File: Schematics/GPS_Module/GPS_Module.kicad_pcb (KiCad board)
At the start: 4 copper layers, 69.5 x 60 mm, 68 parts, among them J1 470804001, J2 SWD_01x04_Pin, J4 Stack Male Edge Connector, J6 USB_B_Micro, Q1 AO3400A, SW1 SW_STM_RESET, SW2 SW_STM_BOOT_MODE, U1 STM32F103CBTx, U10 AMS1117-3.3, U3 W25Q128JVS, U4 LM66100DCKR, U5 LM66100DCKR, U6 LM66100DCKR, U7 ACS70331EOLC, U9 ISO1042BQDWVR, Y1 X322516MMB4SI

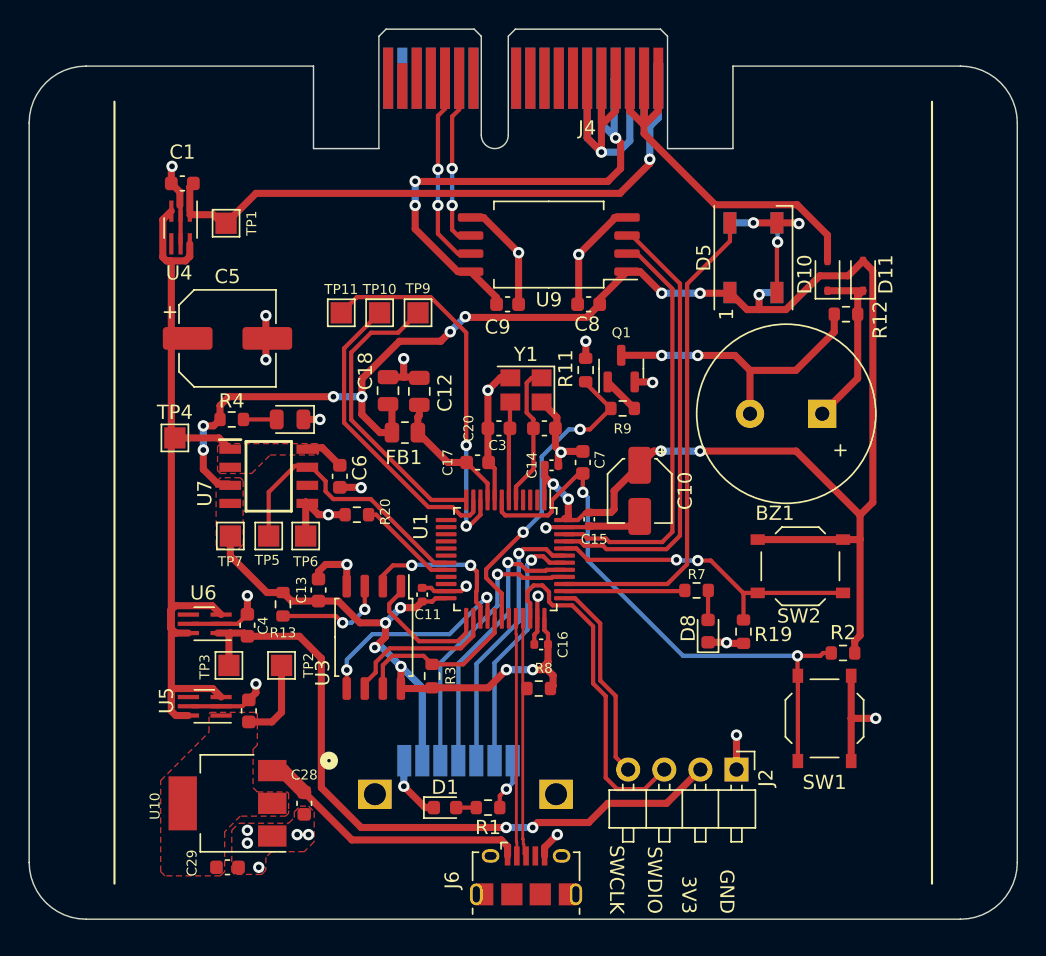
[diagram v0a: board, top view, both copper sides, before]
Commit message: finished silkscreen for GPS module
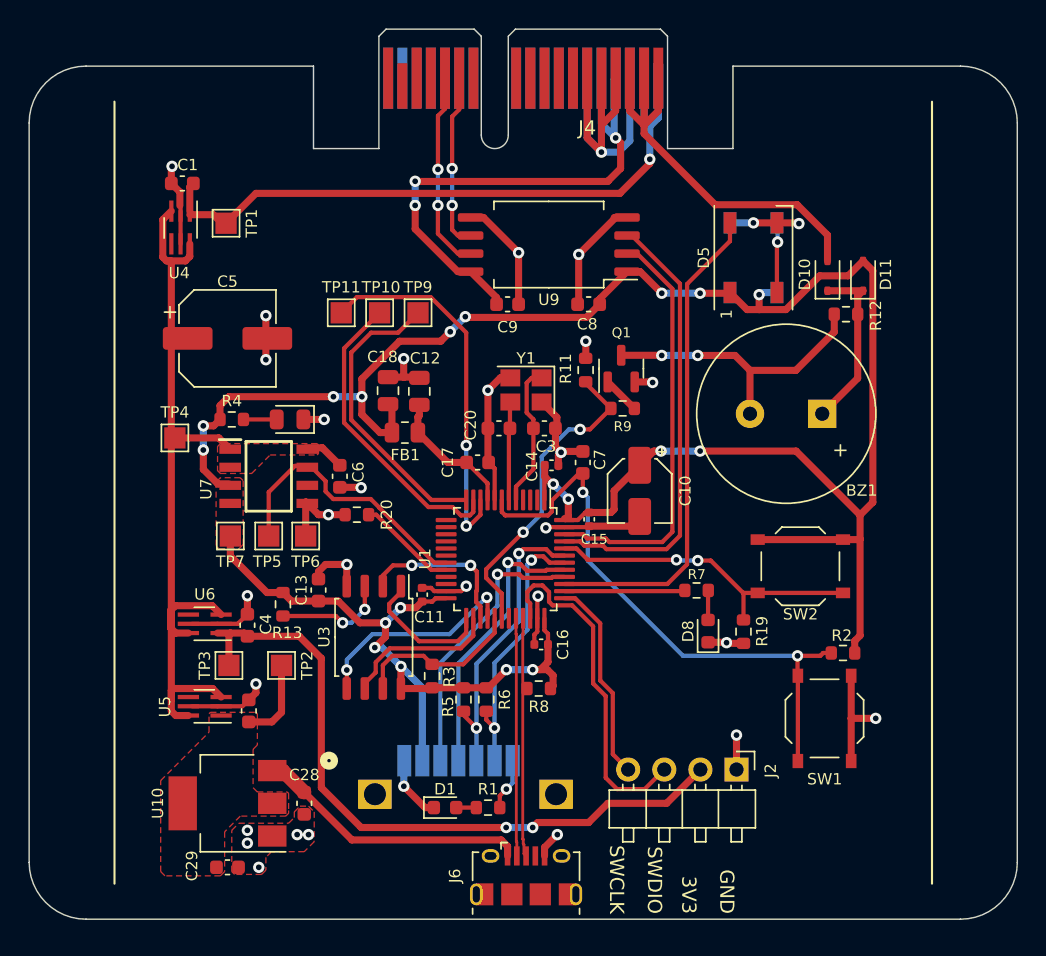
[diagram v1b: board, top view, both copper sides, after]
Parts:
- added R5: 2.2k, Resistor_SMD:R_0603_1608Metric, F.Cu at (52.7, 64.7)
- added R6: 2.2k, Resistor_SMD:R_0603_1608Metric, F.Cu at (54.3, 64.7)
- J1: value 470804001 -> SATA Conn. (Male)
- U1: value STM32F103CBTx -> STM32F103CBT6
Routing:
- net SDA_GPS: track 19.3 -> 20.9 mm, vias 1 -> 2
- net SCL_GPS: track 17.8 -> 19.2 mm, vias 1 -> 2

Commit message: PCB Adjustments + Add USB-C port (DRC pass)
- Rerouted several traces to reduce via hopping
- Routed CANBUS wires as differential pair
- Rearranged some items
- Swapped USB-MicroB port for USB-C port
- Added silkscreen labels
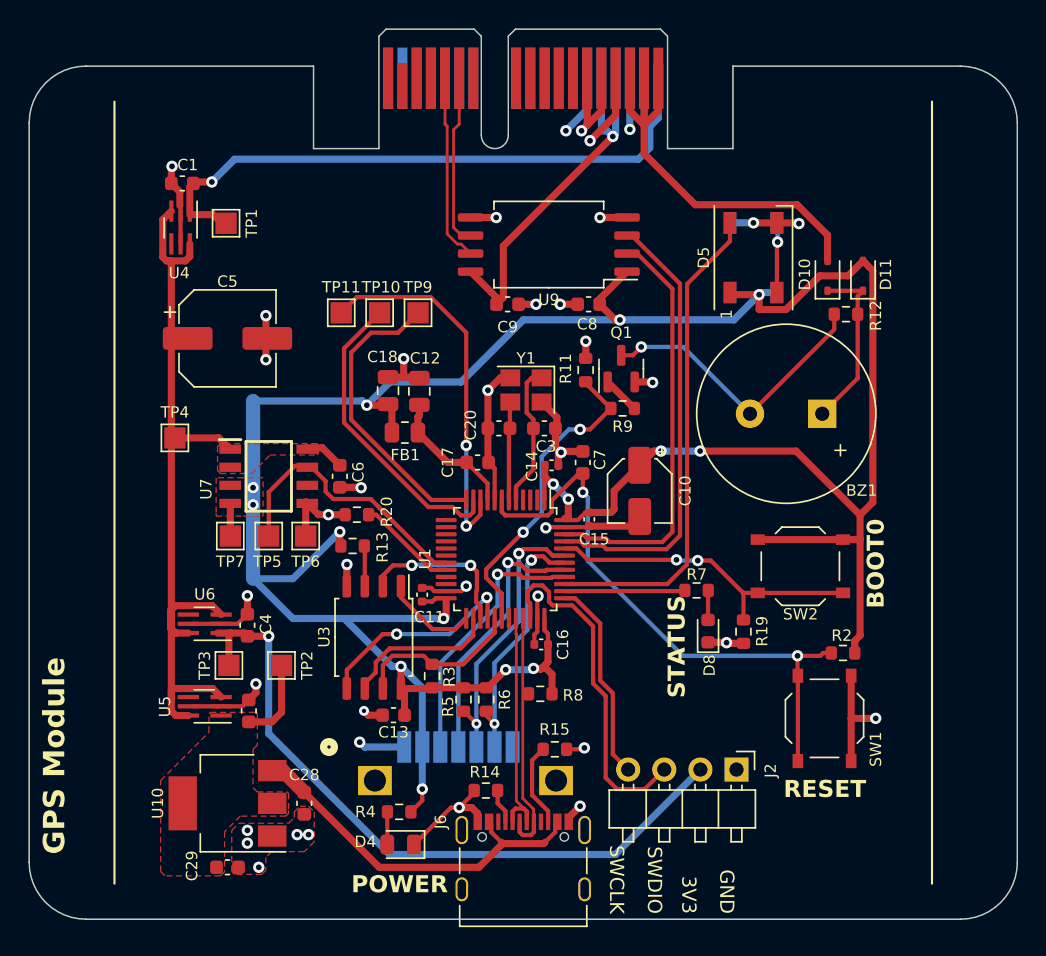
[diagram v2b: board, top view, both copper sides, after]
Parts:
- removed D1: PPS_LED (YLW), LED_SMD:LED_0603_1608Metric
- removed R1: 560R, Resistor_SMD:R_0603_1608Metric
- added R14: 5.1k, Resistor_SMD:R_0603_1608Metric, F.Cu at (54.3, 71.1)
- added R15: 5.1k, Resistor_SMD:R_0603_1608Metric, F.Cu at (59.1, 68.2)
- J6: value USB_B_Micro -> USB_C_Female_USB2_Small; footprint Connector_USB:USB_Micro-B_Amphenol_10118194_Horizontal -> footprints:USB_C_DB-108PWB
- moved D4 30.9 mm to (48.3, 74.9)
- moved R4 30.0 mm to (48.2, 72.6), turned to 0 degrees
- moved C13 10.3 mm to (47.8, 65.8), turned to 180 degrees
- moved R13 6.39 mm to (44.9, 53.9), turned to 180 degrees
- moved J6 1.31 mm to (56.9, 75.8)
- moved J1 0.96 mm to (52.8, 72.9)
- moved R8 0.39 mm to (58.1, 64.3), turned to 180 degrees
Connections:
- J1 pad 7: Net-(J1-Pad7) -> unconnected-(J1-Pad7)
- R8 pad 1: USB_D+ -> +3.3V
- R8 pad 2: +3.3V -> USB_D+
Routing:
- net +3.3V: track 185.2 -> 206.1 mm, vias 19 -> 15
- net GND: track 136.4 -> 122.3 mm, vias 32 -> 38
- net +5V: track 37.6 -> 27.1 mm, vias 3 -> 1
- net /USB_5V: track 19.4 -> 26.5 mm
- net Net-(J6-CC2): track 0.00 -> 5.89 mm
- net Net-(U3-IO2): track 7.98 -> 2.84 mm, vias 2 -> 0
- net Net-(J1-Pad7): track 3.67 -> 0.00 mm, vias 1 -> 0
- net CS_FL: track 9.67 -> 6.63 mm
- net Net-(J6-CC1): track 0.00 -> 2.43 mm
- net Net-(D1-A): track 1.41 -> 0.00 mm
- net +BATT: track 29.0 -> 29.8 mm
- net CAN_H: track 14.0 -> 13.2 mm, vias 2 -> 0
- net USB_D-: track 16.7 -> 17.3 mm
- net V_SWD: track 48.9 -> 49.1 mm, vias 2 -> 1
- net CAN_L: track 12.3 -> 12.1 mm, vias 2 -> 0
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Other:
- board text added: "BOOT0"
- board text added: "GPS Module"
- board text added: "POWER"
- board text added: "RESET"
- board text added: "STATUS"

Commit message: Add silkscreen & final PCB adjustments
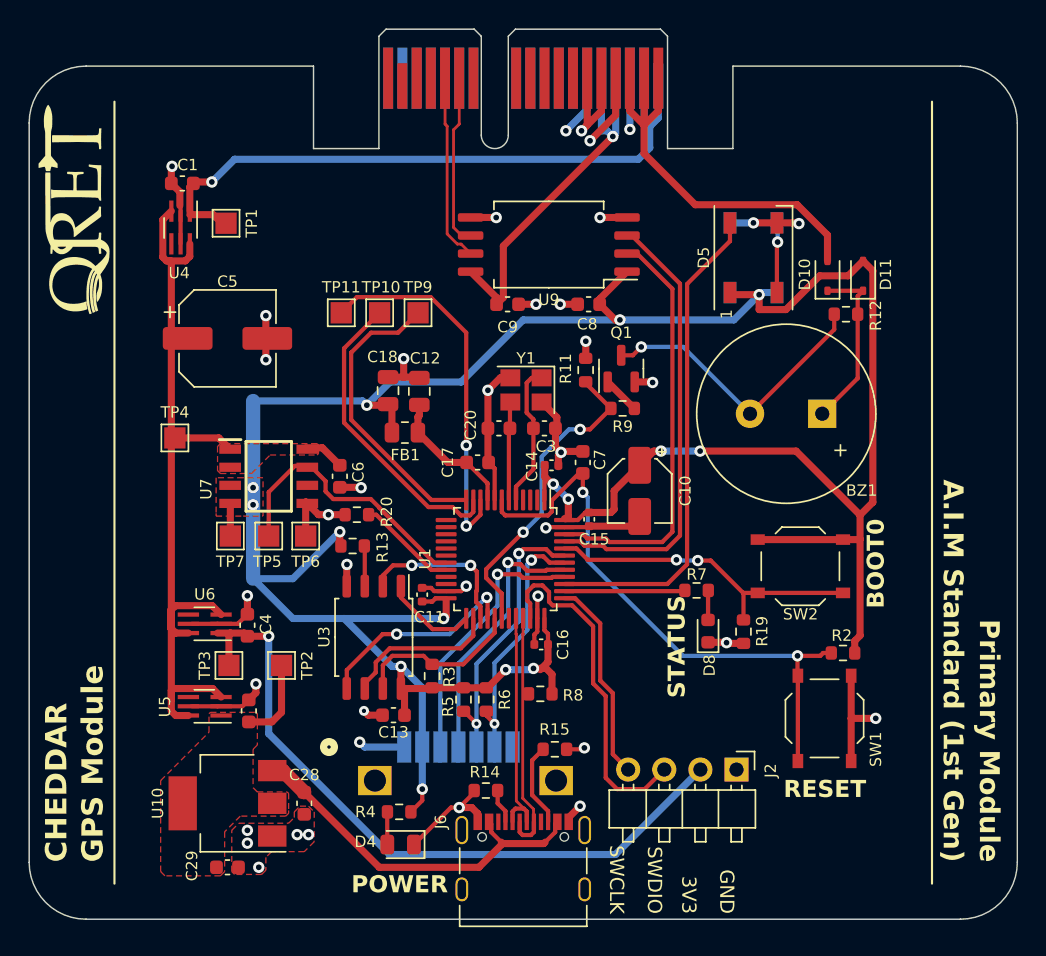
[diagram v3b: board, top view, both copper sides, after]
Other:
- board text added: "A.I.M Standard (1st Gen)"
- board text added: "CHEDDAR"
- board text added: "Cheddar Rev 1.0 QRET Mar 2024 Tristan Alderson Kennan Bays"
- board text added: "Primary Module"
- board text added: "To GPS Antenna Board"

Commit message: Updated Debug/PPS/Power LED resistors
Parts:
- R4: value 820R -> 1.2k
- R7: value 560R -> 680R
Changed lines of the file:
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@@
     (descr "Resistor SMD 0603 (1608 Metric), square (rectangular) end terminal, IPC_7351 nominal, (Body size source: IPC-SM-782 page 72, https://www.pcb-3d.com/wordpress/wp-content/uploads/ipc-sm-782a_amendment_1_and_2.pdf), generated with kicad-footprint-generator")
     (tags "resistor")
-    (property "LCSC" "C23253")
+    (property "LCSC" "C22765")
     (property "Sheetfile" "GPS_Module.kicad_sch")
     (property "Sheetname" "")
@@
         (effects (font (size 0.8 0.8) (thickness 0.1)))
     )
-    (fp_text value "820R" (at 0 1.43) (layer "F.Fab")
+    (fp_text value "1.2k" (at 0 1.43) (layer "F.Fab")
         (effects (font (size 1 1) (thickness 0.15)))
     )
@@
     (descr "Resistor SMD 0603 (1608 Metric), square (rectangular) end terminal, IPC_7351 nominal, (Body size source: IPC-SM-782 page 72, https://www.pcb-3d.com/wordpress/wp-content/uploads/ipc-sm-782a_amendment_1_and_2.pdf), generated with kicad-footprint-generator")
     (tags "resistor")
-    (property "LCSC" "C23204")
+    (property "LCSC" "C23228")
     (property "Sheetfile" "GPS_Module.kicad_sch")
     (property "Sheetname" "")
@@
         (effects (font (size 0.8 0.8) (thickness 0.1)))
     )
-    (fp_text value "560R" (at 0 1.43) (layer "F.Fab")
+    (fp_text value "680R" (at 0 1.43) (layer "F.Fab")
         (effects (font (size 1 1) (thickness 0.15)))
     )
@@
     (polygon
       (pts
-        (xy 22.15 20.15)
-        (xy 91.65 20.15)
+        (xy 22.15 14.15)
+        (xy 91.65 14.15)
         (xy 91.65 80.15)
         (xy 22.15 80.15)

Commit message: Final Revisions
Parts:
- moved D8 1.51 mm to (69.9, 61.4)
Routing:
- net Net-(D8-A): track 2.08 -> 3.59 mm
- net GND: track 122.3 -> 123.0 mm
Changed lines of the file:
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@@
   )
   (footprint "LED_SMD:LED_0603_1608Metric" (layer "F.Cu")
-    (at 69.9 59.8875 90)
+    (at 69.9 61.4 90)
     (descr "LED SMD 0603 (1608 Metric), square (rectangular) end terminal, IPC_7351 nominal, (Body size source: http://www.tortai-tech.com/upload/download/2011102023233369053.pdf), generated with kicad-footprint-generator")
     (tags "LED")
@@
   (segment (start 55.291352 42.0755) (end 54.416352 42.9505) (width 0.5) (layer "F.Cu") (net 1))
   (segment (start 37.5 57.4) (end 37.5 58.7) (width 0.5) (layer "F.Cu") (net 1))
+  (segment (start 71.2 60.7) (end 71.2 60.8875) (width 0.5) (layer "F.Cu") (net 1))
   (segment (start 32.75 29) (end 32.75 29.96005) (width 0.5) (layer "F.Cu") (net 1))
   (segment (start 71.2 60.7) (end 71.2505 60.7505) (width 0.5) (layer "F.Cu") (net 1))
@@
   (segment (start 62.4 23.3) (end 61 24.7) (width 0.5) (layer "F.Cu") (net 1))
   (segment (start 37.15 65.175) (end 35.4 65.175) (width 0.3) (layer "F.Cu") (net 1))
+  (segment (start 71.2 60.8875) (end 69.9 62.1875) (width 0.5) (layer "F.Cu") (net 1))
   (segment (start 79.966352 66.0255) (end 79.966352 63.0255) (width 0.5) (layer "F.Cu") (net 1))
   (segment (start 38.1 63.6) (end 38.1 64.225) (width 0.5) (layer "F.Cu") (net 1))
@@
   (segment (start 76.241352 31.1755) (end 76.291352 31.2255) (width 0.5) (layer "F.Cu") (net 1))
   (segment (start 32.15 28.4) (end 32.15 27.25) (width 0.5) (layer "F.Cu") (net 1))
-  (segment (start 71.175 60.675) (end 71.2 60.7) (width 0.5) (layer "F.Cu") (net 1))
   (segment (start 54.891352 48.4505) (end 54.466352 48.0255) (width 0.3) (layer "F.Cu") (net 1))
-  (segment (start 69.9 60.675) (end 71.175 60.675) (width 0.5) (layer "F.Cu") (net 1))
   (segment (start 59.803852 52.5755) (end 58.541352 52.5755) (width 0.3) (layer "F.Cu") (net 1))
   (segment (start 61.3 40.691852) (end 61.291352 40.7005) (width 0.5) (layer "F.Cu") (net 1))
@@
   (segment (start 67.035557 56.5755) (end 68.424896 55.186161) (width 0.3) (layer "F.Cu") (net 19))
   (segment (start 71.441352 31.1755) (end 71.441352 32.458648) (width 0.3) (layer "F.Cu") (net 19))
-  (segment (start 69.9 57.041852) (end 69.916352 57.0255) (width 0.3) (layer "F.Cu") (net 20))
-  (segment (start 69.9 59.1) (end 69.9 57.041852) (width 0.3) (layer "F.Cu") (net 20))
+  (segment (start 69.916352 57.0255) (end 69.916352 60.596148) (width 0.3) (layer "F.Cu") (net 20))
+  (segment (start 69.916352 60.596148) (end 69.9 60.6125) (width 0.3) (layer "F.Cu") (net 20))
   (segment (start 62.7 70.2) (end 62.7 64.454492) (width 0.3) (layer "F.Cu") (net 22))
   (segment (start 61.816352 59.5505) (end 60.341352 58.0755) (width 0.3) (layer "F.Cu") (net 22))

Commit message: Bump revision number to V2.0 & V1.2
GPS module is V2.0, Antenna PCB is V1.2
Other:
- board text added: "Cheddar Rev 2.0 QRET Feb 2025 Tristan Alderson Kennan Bays"
- board text removed: "Cheddar Rev 1.0 QRET Mar 2024 Tristan Alderson Kennan Bays"
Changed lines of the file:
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@@
   (gr_line (start 42.15 25.95) (end 42.15 20.15)
     (stroke (width 0.1) (type default)) (layer "Edge.Cuts"))
-  (gr_text "Cheddar Rev 1.0\nQRET Mar 2024\n\nTristan Alderson\nKennan Bays" (at 56.9 31.2) (layer "B.SilkS")
+  (gr_text "Cheddar Rev 2.0\nQRET Feb 2025\n\nTristan Alderson\nKennan Bays" (at 56.9 31.2) (layer "B.SilkS")
     (effects (font (size 1.5 1.5) (thickness 0.25)) (justify top mirror))
   )
